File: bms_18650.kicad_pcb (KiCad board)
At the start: 2 copper layers, 35.8 x 35.8 mm, 9 parts, among them IC1 BQ298000RUGR, IC2 EFC8811R-TF

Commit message: first ordered revision
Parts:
- added J2: ~, Library:CELL_LEAD_CONN, F.Cu at (150.0, 100.0)
- IC1: value BQ298000RUGR -> BQ298218RUGR
- moved IC1 54.4 mm to (151.3, 103.0), turned to 0 degrees
- moved IC2 43.1 mm to (146.5, 96.2)
- moved J1 40.0 mm to (150.0, 100.0)
- moved R5 20.1 mm to (154.5, 103.5), turned to -90 degrees
- moved R3 18.3 mm to (152.5, 97.5), turned to 90 degrees
- moved R4 14.6 mm to (150.5, 94.5), turned to 90 degrees
- moved C2 13.0 mm to (149.0, 106.0)
- moved R_SEN1 12.7 mm to (147.5, 104.0), turned to 180 degrees
- moved C1 12.0 mm to (148.0, 100.0), turned to 180 degrees
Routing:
- net CELL-: track 0.00 -> 28.5 mm, vias 0 -> 3
- net LINK+: track 0.00 -> 21.6 mm, vias 0 -> 4
- net CELL+: track 0.00 -> 19.4 mm
- net Net-(IC1-VDD): track 0.00 -> 15.4 mm, vias 0 -> 3
- net Net-(IC1-DSG): track 0.00 -> 11.5 mm, vias 0 -> 2
- net Net-(IC1-CHG): track 0.00 -> 11.1 mm, vias 0 -> 2
- net Net-(IC1-BAT): track 0.00 -> 8.39 mm
- net Net-(IC1-CS): track 0.00 -> 3.60 mm
- net Net-(IC1-PACK): track 0.00 -> 3.12 mm
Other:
- board size 35.8 x 35.8 mm -> 16 x 16 mm
- copper layers 2 -> 4
- board text added: "ataboi"

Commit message: add readme
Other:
- board text added: "+"
- board text added: "-"
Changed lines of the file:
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@@
 			(drillshape 0)
 			(scaleselection 1)
-			(outputdirectory "gerbers/")
+			(outputdirectory "fab/gerbers/")
 		)
 	)
@@
 			(at 0 0.307 0)
 			(layer "F.SilkS")
+			(hide yes)
 			(effects
 				(font
@@
 			(at -0.15 0 0)
 			(layer "F.SilkS")
+			(hide yes)
 			(effects
 				(font
@@
 			)
 			(justify left bottom)
+		)
+	)
+	(gr_text "-"
+		(at 142.040207 100.914761 0)
+		(layer "F.SilkS")
+		(effects
+			(font
+				(size 2 1)
+				(thickness 0.2)
+				(bold yes)
+			)
+			(justify left bottom)
+		)
+	)
+	(gr_text "+"
+		(at 156.498904 100.532473 0)
+		(layer "F.SilkS")
+		(effects
+			(font
+				(size 1 1)
+				(thickness 0.2)
+				(bold yes)
+			)
+			(justify left bottom)

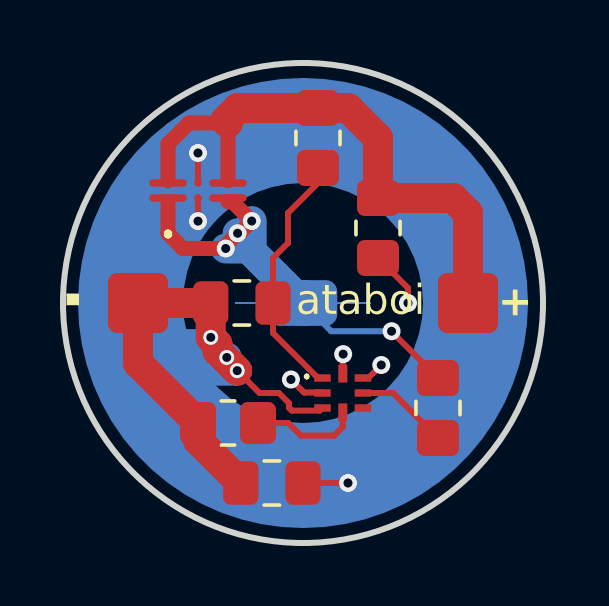
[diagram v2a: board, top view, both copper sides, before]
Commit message: no more blind vias
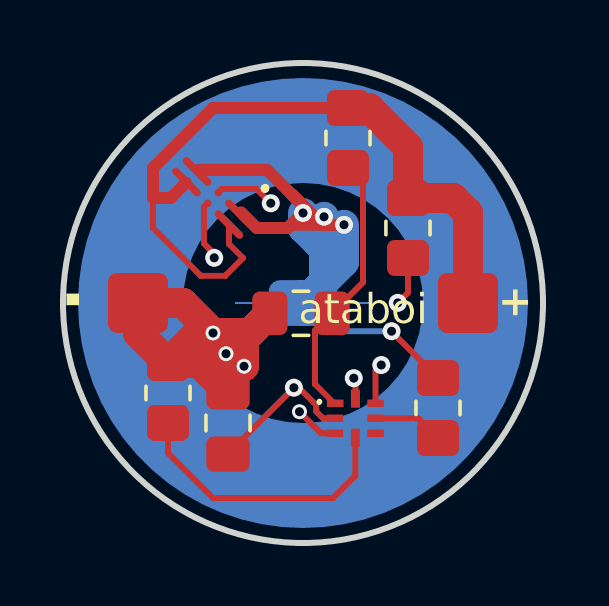
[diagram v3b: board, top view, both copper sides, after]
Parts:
- moved C2 2.48 mm to (147.5, 104.0), turned to -90 degrees
- moved R_SEN1 2.24 mm to (145.5, 103.0), turned to 90 degrees
- moved C1 2.00 mm to (149.9, 100.3)
- moved R3 1.00 mm to (153.5, 97.5)
- moved R4 1.00 mm to (151.5, 94.5)
- moved IC1 0.94 mm to (151.7, 103.8)
- moved IC2 0.56 mm to (147.0, 96.5), turned to 135 degrees
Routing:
- net CELL-: track 28.5 -> 34.7 mm, vias 3 -> 4
- net LINK+: track 21.6 -> 27.6 mm
- net CELL+: track 19.4 -> 25.3 mm
- net Net-(IC1-CS): track 3.60 -> 9.44 mm
- net Net-(IC1-CHG): track 11.1 -> 9.03 mm
- net Net-(IC1-DSG): track 11.5 -> 10.3 mm
- net Net-(IC1-VDD): track 15.4 -> 14.2 mm, vias 3 -> 2
- net Net-(IC1-PACK): track 3.12 -> 2.35 mm
- net Net-(IC1-BAT): track 8.39 -> 9.01 mm

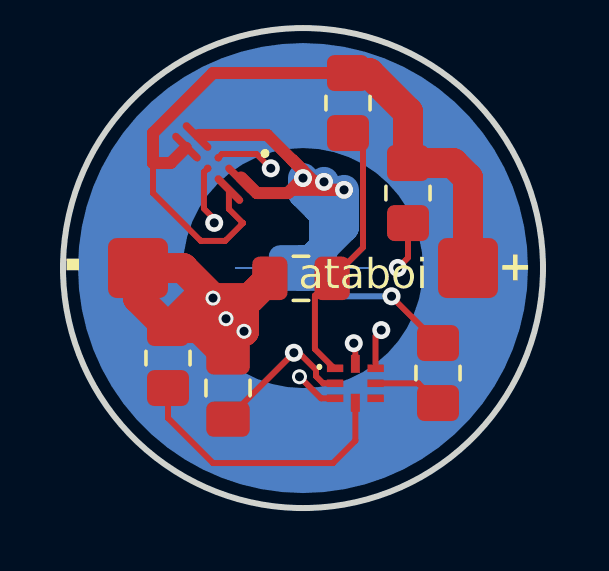
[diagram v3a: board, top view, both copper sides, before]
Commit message: fix footprint
fixes issue #1
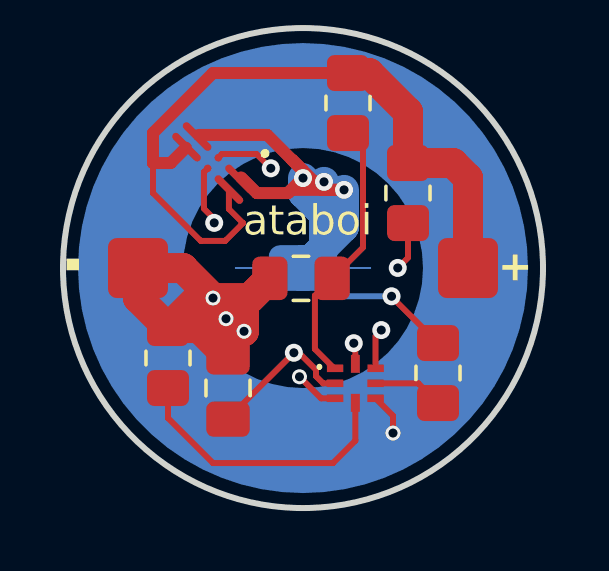
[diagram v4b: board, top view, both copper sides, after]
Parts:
- C1, C2: value 0.1uF -> 100n
- R3: value 330 -> 330R
- R4: value 20 -> 20R
- R5: value 2k -> 2K
- R_SEN1: value 0.001 -> 0R001
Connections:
- IC1 pad 5: unconnected-(IC1-CTR-Pad5) -> CELL-
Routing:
- net CELL-: track 34.7 -> 41.3 mm, vias 4 -> 5
